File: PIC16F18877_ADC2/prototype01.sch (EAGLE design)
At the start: 25 parts, among them CN1 PIC_CN_H, CN2 ADC_IN, CN3 UART_IF, CN4 AE-MICRO-SD-DIP, SW1 10-XX, U1 PIC16F18877-I/P, U2 AE-AQM1602A

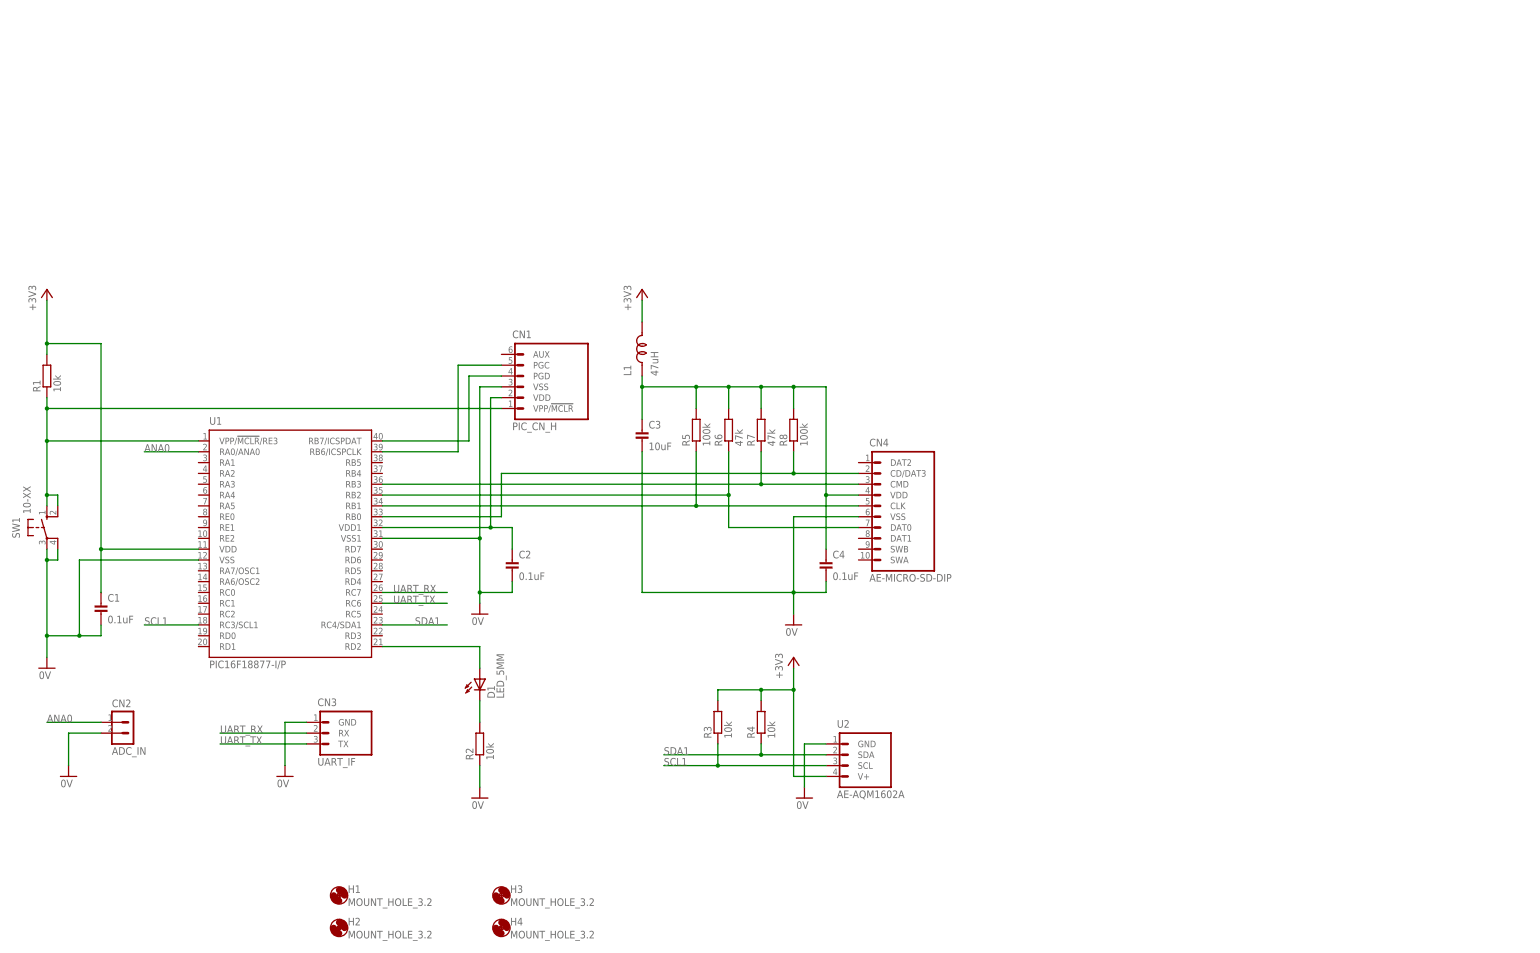
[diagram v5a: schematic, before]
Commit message: 回路図を修正
リアルタイムクロックモジュールを増設
（microSDカードのファイルタイムスタンプを正しく設定するための措置）
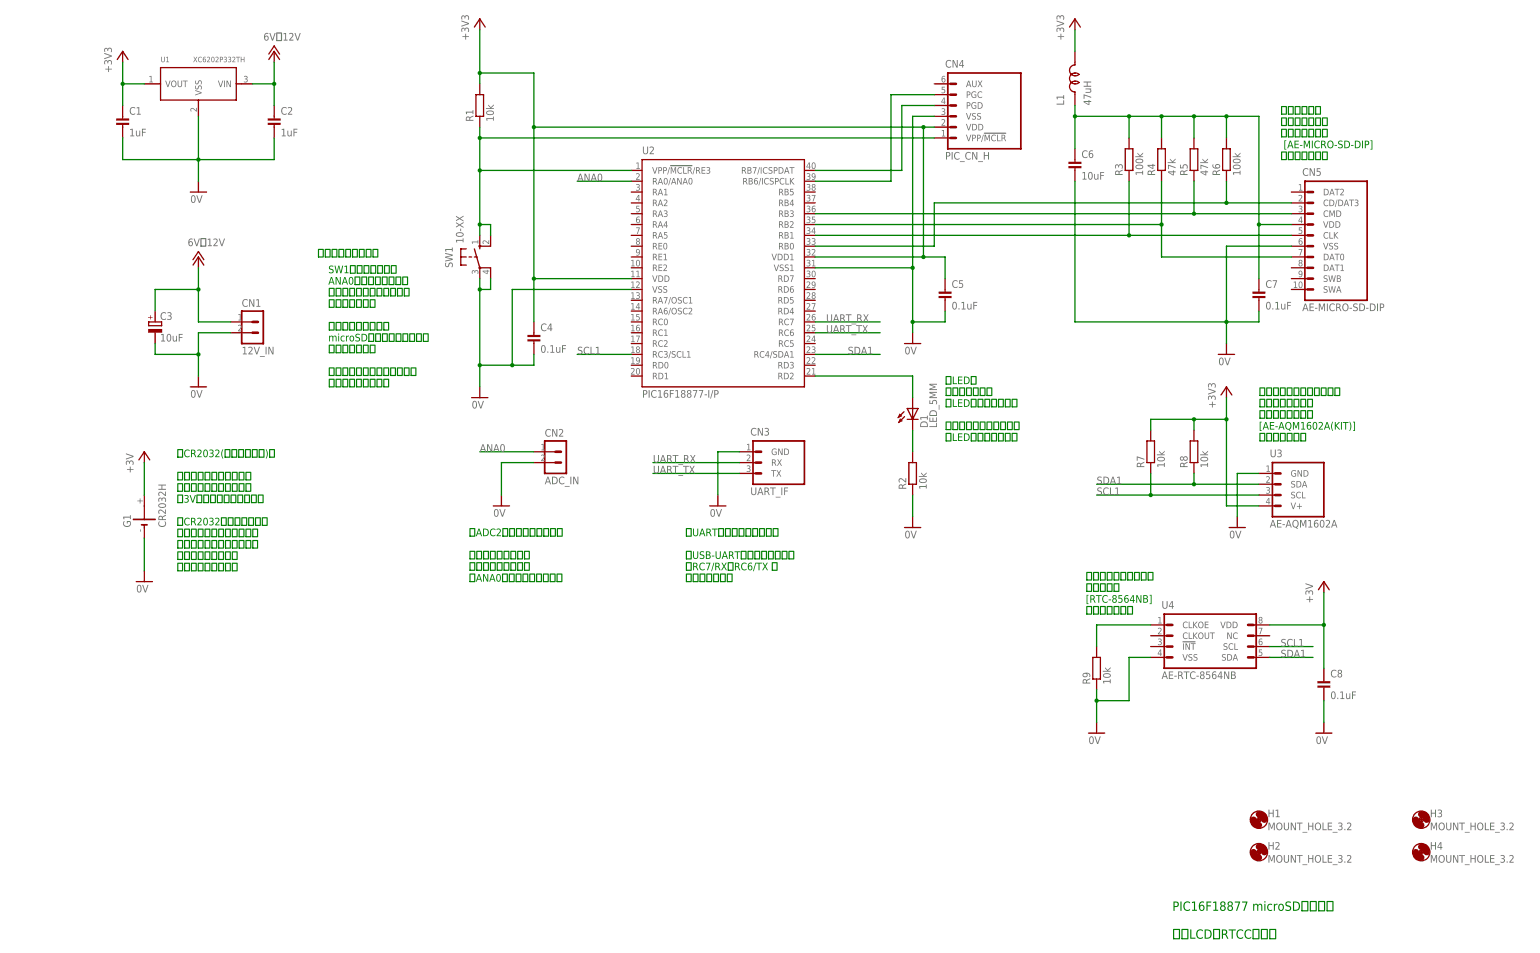
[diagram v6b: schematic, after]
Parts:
- added C5, C7, C8: 0.1uF, Parts:CAP_200MIL
- added C6: 10uF, Parts:CAP_200MIL
- added CN5: AE-MICRO-SD-DIP, PartsForProto:AE-MICRO-SD-DIP
- added G1: CR2032H, Parts:CR2032H
- added R9: 10k, Parts:RESISTOR_300MIL
- added U3: AE-AQM1602A, PartsForProto:AE-AQM1602A
- added U4: AE-RTC-8564NB, PartsForProto:AE-RTC-8564NB
- C1, C2: value 0.1uF -> 1uF
- C3: device Parts:CAP_200MIL -> Parts:ELECAP_200MIL
- CN1: value PIC_CN_H -> 12V_IN; device Connectors:PIC_CN_H -> Connectors:CONN_2PIN-L
- CN4: value AE-MICRO-SD-DIP -> PIC_CN_H; device PartsForProto:AE-MICRO-SD-DIP -> Connectors:PIC_CN_H
- R3: value 10k -> 100k
- R4: value 10k -> 47k
- R5: value 100k -> 47k
- R6: value 47k -> 100k
- R7: value 47k -> 10k
- R8: value 100k -> 10k
- U1: value PIC16F18877-I/P -> XC6202P332TH; device Parts:PIC16F18877-I/P -> Parts:XC6202P332TH
- U2: value AE-AQM1602A -> PIC16F18877-I/P; device PartsForProto:AE-AQM1602A -> Parts:PIC16F18877-I/P
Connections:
- removed net N$10: C2.1, CN1.VDD, U1.VDD1
- new net +12V: C2.1, C3.+, CN1.1, U1.VIN
- new net +3V: C8.1, G1.+, U4.VDD
- new net N$16: R9.2, U4.CLKOE
- net +3V3: now also C4.1, C5.1, CN4.VDD, R7.2, R8.2, U1.VOUT, U2.VDD, U2.VDD1, U3.V+; no longer R3.2, R4.2, U1.VDD, U2.V+
- net 0V: now also C3.-, C5.2, C6.2, C7.2, C8.2, CN1.2, CN5.VSS, G1.-, R9.1, U2.VSS, U2.VSS1, U3.GND, U4.VSS; no longer C3.2, CN1.VSS, U1.VSS1, U2.GND
- net ANA0: now also U2.RA0/ANA0; no longer U1.RA0/ANA0
- net N$12: now also CN5.CMD, R5.1, U2.RB3; no longer CN4.CMD, R7.1, U1.RB3
- net N$2: now also CN4.PGD, U2.RB7/ICSPDAT; no longer CN1.PGD, U1.RB7/ICSPDAT
- net N$3: now also CN4.VPP/!MCLR, U2.VPP/!MCLR!/RE3; no longer CN1.VPP/!MCLR, U1.VPP/!MCLR!/RE3
- net N$4: now also CN4.PGC, U2.RB6/ICSPCLK; no longer CN1.PGC, U1.RB6/ICSPCLK
- net N$5: now also U2.RD2; no longer U1.RD2
- net N$6: now also CN5.CLK, R3.1, U2.RB1; no longer CN4.CLK, R5.1, U1.RB1
- net N$7: now also CN5.CD/DAT3, R6.1, U2.RB0; no longer CN4.CD/DAT3, R8.1, U1.RB0
- net N$8: now also CN5.DAT0, R4.1, U2.RB2; no longer CN4.DAT0, R6.1, U1.RB2
- net N$9: now also C6.1, C7.1, CN5.VDD, R3.2, R4.2; no longer C3.1, C4.1, CN4.VDD, R7.2, R8.2
- net SCL1: now also R7.1, U2.RC3/SCL1, U3.SCL, U4.SCL; no longer R3.1, U1.RC3/SCL1, U2.SCL
- net SDA1: now also R8.1, U2.RC4/SDA1, U3.SDA, U4.SDA; no longer R4.1, U1.RC4/SDA1, U2.SDA
- net UART_RX: now also U2.RC7; no longer U1.RC7
- net UART_TX: now also U2.RC6; no longer U1.RC6
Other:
- note added: "PIC16F18877 microSDサンプル 小型LCD／RTCCを接続"
- note added: "SW1：ボタン押下で ANA0端子に接続された アナログ出力の電圧測定が 開始されます。 測定値は１秒ごとに microSDカードのファイルへ 出力されます。 測定中にボタン押下すると、 測定を中止します。"
- note added: "【ADC2のご使用について】 センサー等からの アナログ出力を、 ANA0端子に接続します。"
- note added: "【CR2032(ボタン乾電池)】 リアルタイムクロック モジュールには、常時 3Vを給電してください。 CR2032から非給電時に マイコンを起動しても、 リアルタイムクロックは 動作しませんので ご注意ください。"
- note added: "【LED】 電圧測定中は LEDが点灯します。 電圧測定が停止すると LEDが消灯します。"
- note added: "【UARTのご使用について】 USB-UART変換基板などを、 RC7/RX、RC6/TX に 接続します。"
- note added: "【タクトスイッチ】"
- note added: "マイクロＳＤ カードスロット ＤＩＰ化キット [AE-MICRO-SD-DIP] を使用します。"
- note added: "リアルタイムクロック モジュール [RTC-8564NB] を使用します。"
- note added: "Ｉ２Ｃ接続小型キャラクタ ＬＣＤモジュール ピッチ変換キット [AE-AQM1602A(KIT)] を使用します。"
- moved on the sheet: C1, C2, C4, CN2, CN3, D1, H1, H2, H3, H4, L1, R1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

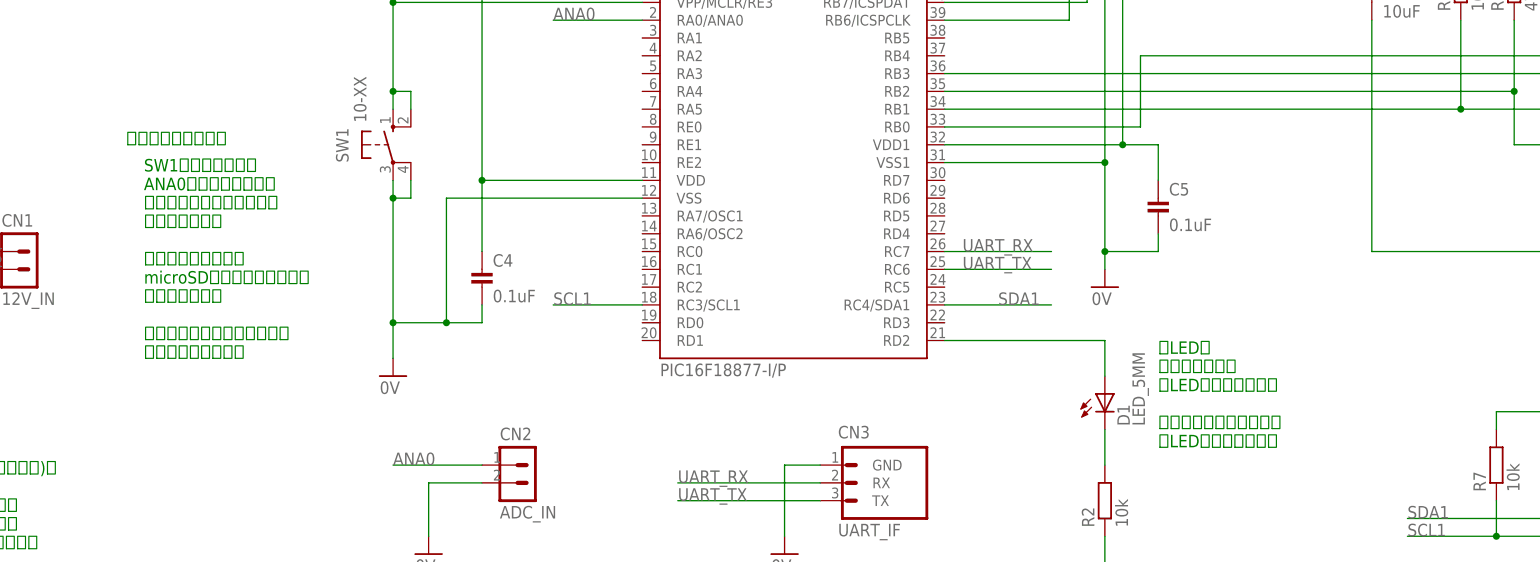
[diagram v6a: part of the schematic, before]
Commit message: 回路図のコメントがおかしいので修正
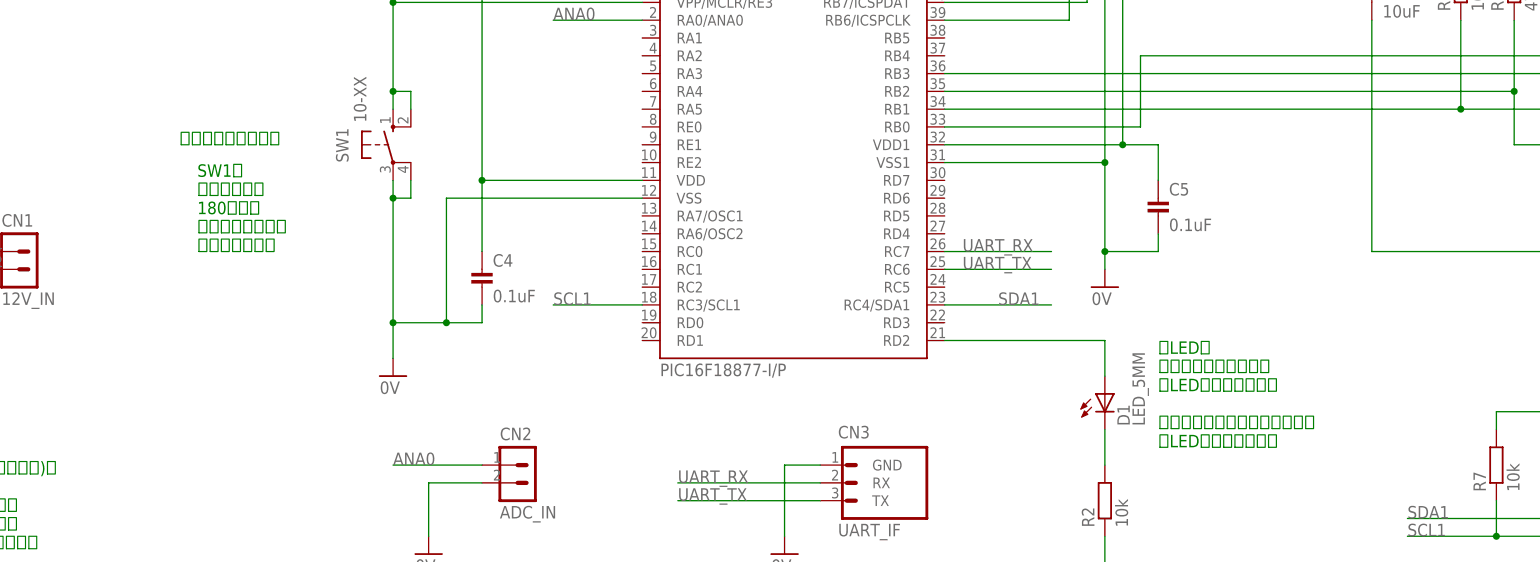
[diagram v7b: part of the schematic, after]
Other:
- note added: "SW1： ボタン押下で 180秒間の カウントダウンが 開始されます。"
- note added: "【LED】 カウントダウン中は LEDが点灯します。 カウントダウンが停止すると LEDが消灯します。"
- note removed: "SW1：ボタン押下で ANA0端子に接続された アナログ出力の電圧測定が 開始されます。 測定値は１秒ごとに microSDカードのファイルへ 出力されます。 測定中にボタン押下すると、 測定を中止します。"
- note removed: "【LED】 電圧測定中は LEDが点灯します。 電圧測定が停止すると LEDが消灯します。"
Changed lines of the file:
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@@
 [RTC-8564NB]
 を使用します。</text>
-<text x="91.44" y="170.18" size="1.778" layer="91">【タクトスイッチ】</text>
+<text x="99.06" y="170.18" size="1.778" layer="91">【タクトスイッチ】</text>
 <text x="58.42" y="96.52" size="1.778" layer="91">【CR2032(ボタン乾電池)】
 　リアルタイムクロック
@@
 　ANA0端子に接続します。</text>
 <text x="238.76" y="127" size="1.778" layer="91">【LED】
-　電圧測定中は
+　カウントダウン中は
 　LEDが点灯します。
-　電圧測定が停止すると
+　カウントダウンが停止すると
 　LEDが消灯します。</text>
-<text x="93.98" y="139.7" size="1.778" layer="91">SW1：ボタン押下で
-ANA0端子に接続された
-アナログ出力の電圧測定が
-開始されます。
-測定値は１秒ごとに
-microSDカードのファイルへ
-出力されます。
-測定中にボタン押下すると、
-測定を中止します。</text>
+<text x="101.6" y="154.94" size="1.778" layer="91">SW1：
+ボタン押下で
+180秒間の
+カウントダウンが
+開始されます。</text>
 </plain>
 <instances>

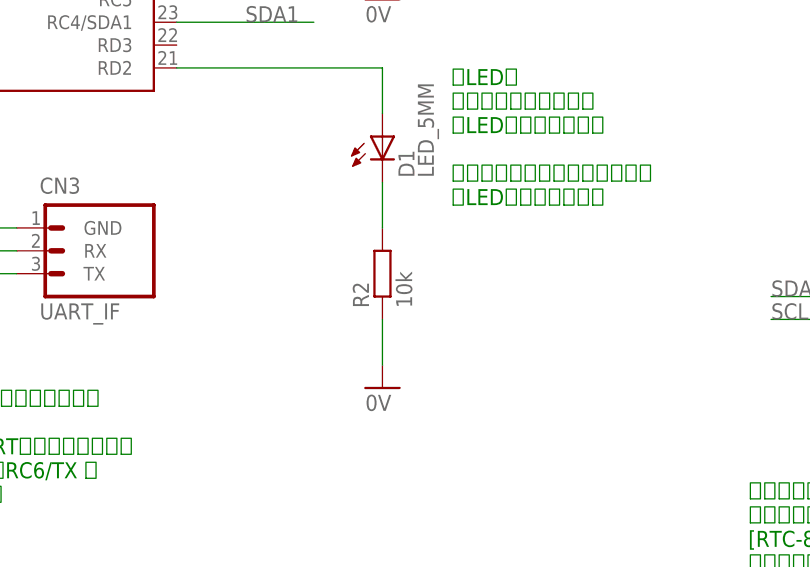
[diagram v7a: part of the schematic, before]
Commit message: 定数修正
LEDの電流制限抵抗値
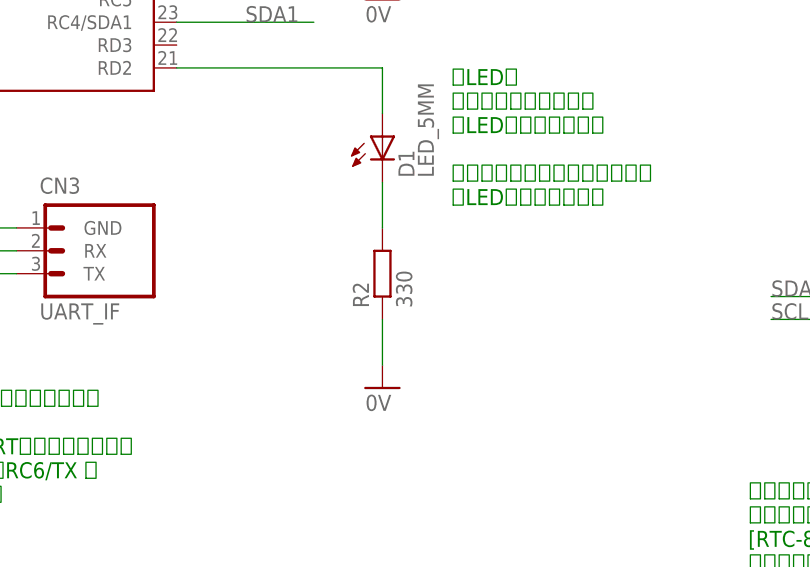
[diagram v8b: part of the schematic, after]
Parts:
- R2: value 10k -> 330
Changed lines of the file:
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@@
 <part name="GND3" library="Supply" deviceset="0V" device=""/>
 <part name="D1" library="Parts" deviceset="LED" device="_5MM"/>
-<part name="R2" library="Parts" deviceset="RESISTOR" device="_300MIL" value="10k"/>
+<part name="R2" library="Parts" deviceset="RESISTOR" device="_300MIL" value="330"/>
 <part name="L1" library="Parts" deviceset="TC5026-22UH-060" device="" value="47uH"/>
 <part name="+3V3" library="Supply" deviceset="+3V3" device=""/>
